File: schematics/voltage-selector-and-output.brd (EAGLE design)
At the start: 55.5 x 30.5 mm, 30 parts, among them IC1 5V, IC2 MIC2941, IC3 MCP41010P, IC5 12V, IC6 ATTINY85, Q1 2N3906

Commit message: Updated the schematics
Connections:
- net PB4: now also IC3.1
- net PB5: no longer IC3.1
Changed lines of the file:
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@@
 <contactref element="ISP" pad="1"/>
 <contactref element="IC6" pad="1"/>
-<contactref element="IC3" pad="1"/>
-<wire x1="6.35" y1="2.54" x2="19.05" y2="2.54" width="0" layer="19" extent="1-1"/>
-<wire x1="1.27" y1="17.78" x2="6.35" y2="2.54" width="0" layer="19" extent="1-1"/>
+<wire x1="6.35" y1="2.54" x2="1.27" y2="17.78" width="0" layer="19" extent="1-1"/>
 </signal>
 <signal name="PB2">
@@
 <contactref element="IC6" pad="3"/>
 <contactref element="JP4" pad="7"/>
-<wire x1="11.43" y1="2.54" x2="46.99" y2="2.54" width="0" layer="19" extent="1-1"/>
+<contactref element="IC3" pad="1"/>
+<wire x1="19.05" y1="2.54" x2="46.99" y2="2.54" width="0" layer="19" extent="1-1"/>
+<wire x1="11.43" y1="2.54" x2="19.05" y2="2.54" width="0" layer="19" extent="1-1"/>
 </signal>
 <signal name="PB0">

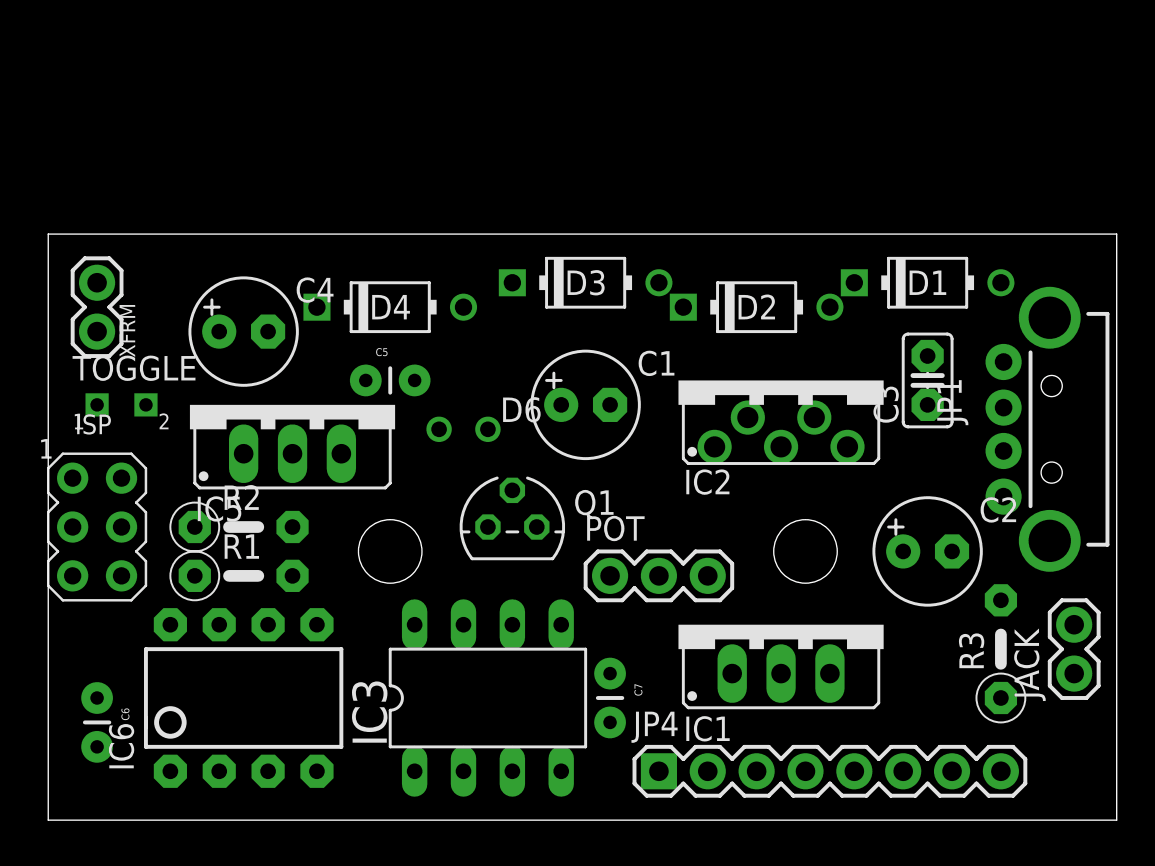
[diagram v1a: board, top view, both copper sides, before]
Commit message: Decided to remove the "adjustable" option because it was kinda useless
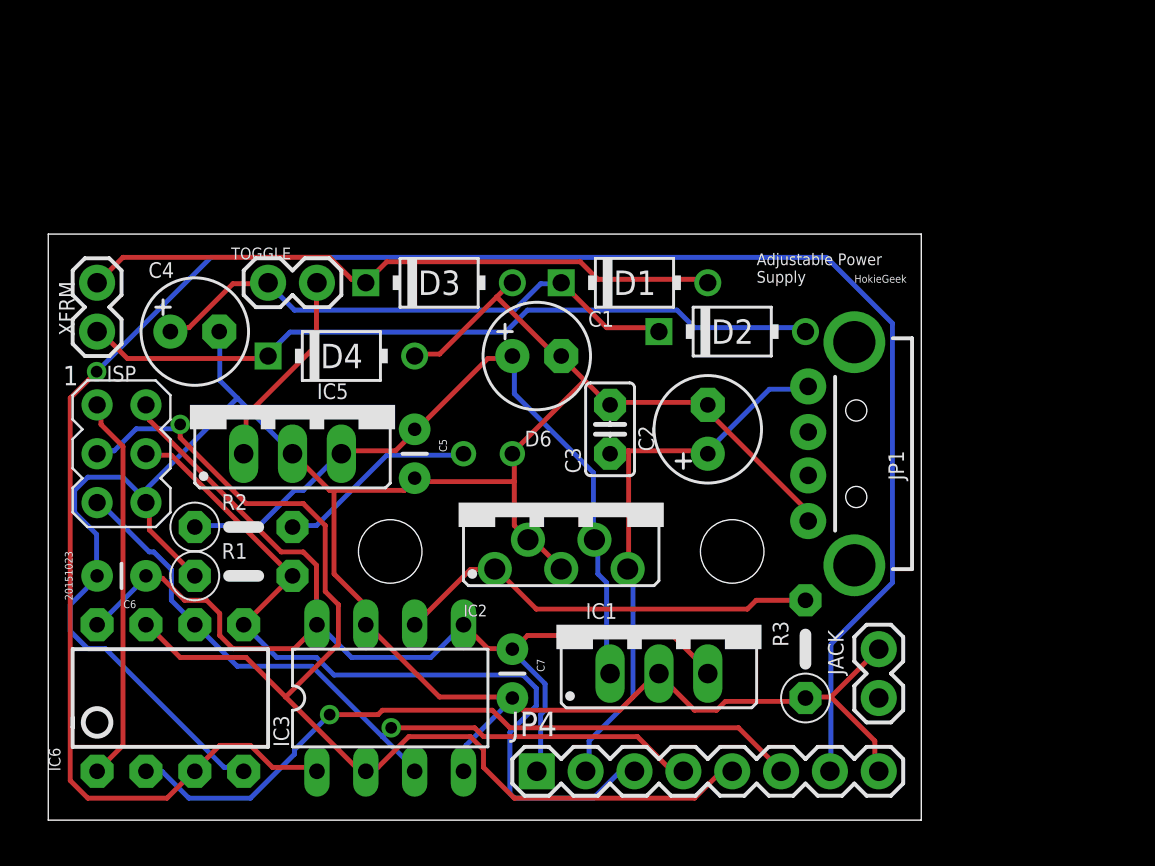
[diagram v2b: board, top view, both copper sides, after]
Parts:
- removed POT: (no value), SparkFun:1X03
- removed Q1: 2N3906, transistor-pnp:TO92
- TOGGLE: value SPST -> (none); device gm-switches:SPST -> SparkFun:1X02
- moved C3 16.7 mm to (29.2, 20.3)
- moved D1 15.2 mm to (30.5, 27.9)
- moved C2 13.1 mm to (34.3, 20.3), turned to 90 degrees
- moved IC2 13.1 mm to (26.7, 16.5)
- moved JACK 10.2 mm to (43.2, 6.35)
- moved JP1 10.2 mm to (41.9, 19.1)
- moved R3 10.2 mm to (39.4, 8.89)
- moved TOGGLE 9.92 mm to (11.4, 27.9)
- moved D3 7.62 mm to (20.3, 27.9)
- moved C6 6.84 mm to (5.08, 12.7), turned to 180 degrees
- moved IC1 6.35 mm to (31.8, 10.2)
- moved JP4 6.35 mm to (25.4, 2.54)
- moved C7 5.24 mm to (24.1, 8.89)
- moved IC3 5.08 mm to (17.8, 6.35)
- moved ISP 4.02 mm to (3.81, 19.1)
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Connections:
- removed net N$5: C1.+, C5.1, IC5.OUT, R2.1
- removed net N$6: POT.2
- removed net N$7: POT.3, Q1.1
- removed net N$8: Q1.2
- new net N$11: JACK.1
- net AGND: now also D6.K; no longer Q1.3
- net RECTIFIED_12VCC: now also C1.+, C5.1, IC5.OUT, R2.1; no longer D6.K
- net VADJ: no longer JACK.1, POT.1
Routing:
- net AGND: track 0.00 -> 148.0 mm
- net PB4: track 0.00 -> 106.7 mm, vias 0 -> 1
- net PB2: track 0.00 -> 62.3 mm, vias 0 -> 1
- net IC_VCC: track 0.00 -> 61.7 mm
- net PB0: track 0.00 -> 43.6 mm
- net PB1: track 0.00 -> 40.1 mm, vias 0 -> 1
- net N$3: track 0.00 -> 39.1 mm
- net RECTIFIED_12VCC: track 0.00 -> 38.9 mm
- net PB3: track 0.00 -> 37.0 mm, vias 0 -> 1
- net N$2: track 0.00 -> 33.9 mm
- net VADJ: track 0.00 -> 29.9 mm
- net N$9: track 0.00 -> 28.8 mm
- net N$4: track 0.00 -> 22.5 mm
- net PB5: track 0.00 -> 20.2 mm
- net N$1: track 0.00 -> 10.5 mm
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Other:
- board size 55.5 x 30.5 mm -> 45.4 x 30.5 mm
- board text added: "20151023"
- board text added: "Adjustable Power Supply"
- board text added: "HokieGeek"

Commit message: Optimizing the location of the components on the board and fixing the schematic
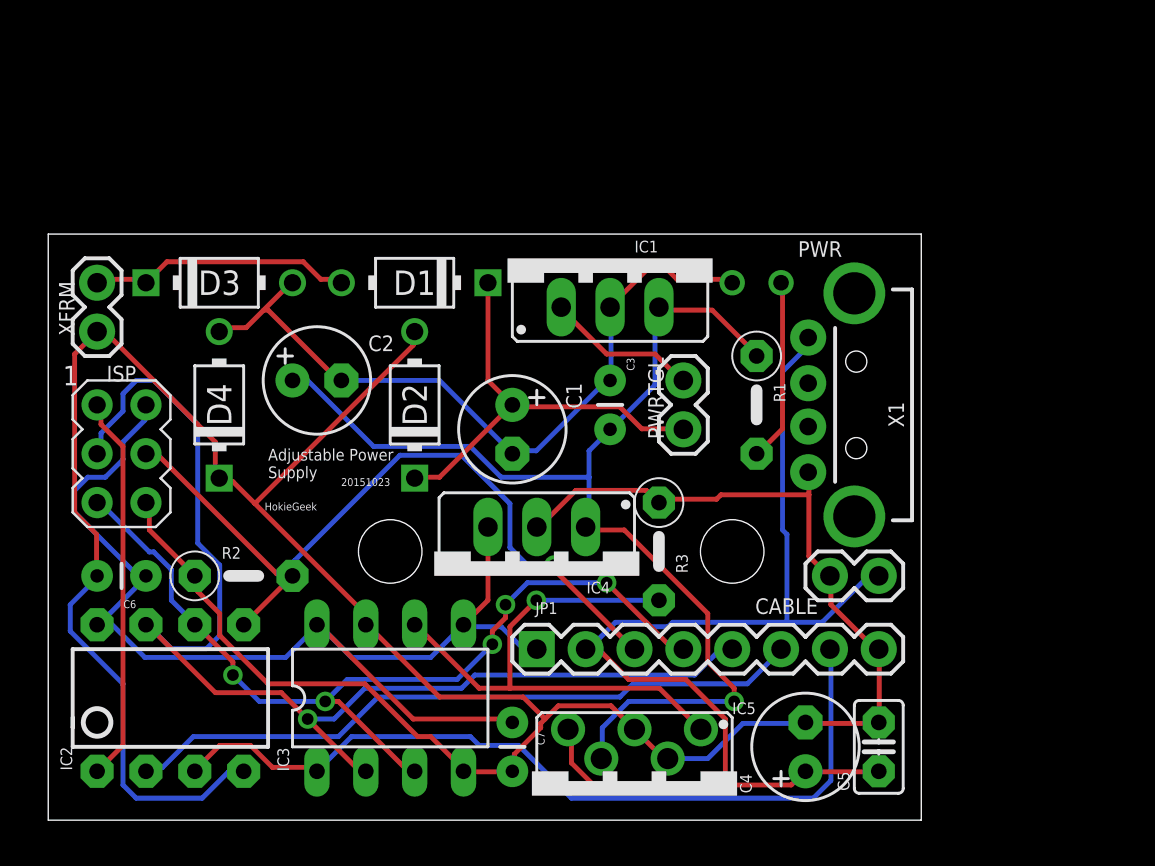
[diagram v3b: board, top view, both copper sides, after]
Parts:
- removed D6: (no value), SparkFun-LED:LED3MM-NS
- removed IC6: ATTINY85, SparkFun:DIP08
- removed JACK, TOGGLE: (no value), SparkFun:1X02
- removed JP4: (no value), SparkFun:1X08
- added CABLE, PWRTGL: (no value), SparkFun:1X02
- added IC4: 5V, v-reg:78XXS
- added PWR: (no value), SparkFun-LED:LED3MM-NS
- added X1: USB-A-H, SparkFun-Connectors:USB-A-H
- C3: device minimidi:C025-025X050 -> SparkFun-Capacitors:CAP-PTH-SMALL
- C5: device SparkFun-Capacitors:CAP-PTH-SMALL -> minimidi:C025-025X050
- IC1: value 5V -> 12V
- IC2: value MIC2941 -> ATTINY85; device bbsup:TO220-5 -> SparkFun:DIP08
- IC5: value 12V -> MIC2941; device v-reg:78XXS -> bbsup:TO220-5
- JP1: value USB-A-H -> (none); device SparkFun-Connectors:USB-A-H -> SparkFun:1X08
- R1: value 10k -> 1k
- R2: value 1k -> 10k
- moved C4 38.4 mm to (39.4, 3.81), turned to 90 degrees
- moved C5 29.2 mm to (43.2, 3.81), turned to 90 degrees
- moved R1 28.1 mm to (36.8, 21.6), turned to 270 degrees
- moved IC5 27.0 mm to (30.5, 1.27), turned to 180 degrees
- moved IC2 22.7 mm to (6.35, 6.35)
- moved C2 20.5 mm to (14.0, 22.9), turned to 0 degrees
- moved JP1 19.4 mm to (25.4, 8.89), turned to 0 degrees
- moved IC1 19.2 mm to (29.2, 29.2)
- moved D2 16.9 mm to (19.1, 21.6), turned to 90 degrees
- moved D1 11.4 mm to (19.1, 27.9), turned to 180 degrees
- moved D3 11.4 mm to (8.89, 27.9)
- moved R3 9.16 mm to (31.8, 14.0), turned to 270 degrees
- moved D4 6.84 mm to (8.89, 21.6), turned to 90 degrees
- moved C1 4.02 mm to (24.1, 20.3), turned to 270 degrees
- moved C7 3.81 mm to (24.1, 5.08)
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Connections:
- removed net N$11: JACK.1
- removed net N$3: D2.A, D4.C, XFRM.1
- new net N$5: C1.-, C2.-, C3.2, D3.A, D4.A, IC1.GND, PWR.K
- net AGND: now also CABLE.2, D2.A, D4.C, IC2.4, IC4.GND, IC5.2, IC5.3, JP1.8, R2.1, X1.GND, XFRM.1; no longer C1.-, C2.-, C3.2, D3.A, D4.A, D6.K, IC1.GND, IC2.2, IC2.3, IC5.GND, IC6.4, JACK.2, JP1.GND, JP4.8, R1.1
- net IC_VCC: now also IC2.8, IC4.OUT, JP1.1; no longer IC1.OUT, IC6.8, JP4.1
- net N$1: now also IC1.IN, PWRTGL.2; no longer IC5.IN, TOGGLE.2
- net N$10: now also PWR.A, R1.2; no longer D6.A, R2.2
- net N$4: now also IC5.1; no longer IC2.1
- net N$9: now also C1.+, PWRTGL.1; no longer C4.+, TOGGLE.1
- net PB0: now also IC2.5, JP1.3, R2.2; no longer IC6.5, JP4.3, R1.2
- net PB1: now also IC2.6, JP1.4; no longer IC6.6, JP4.4
- net PB2: now also IC2.7, JP1.5; no longer IC6.7, JP4.5
- net PB3: now also IC2.2, JP1.6; no longer IC6.2, JP4.6
- net PB4: now also IC2.3, JP1.7; no longer IC6.3, JP4.7
- net PB5: now also IC2.1; no longer IC6.1
- net RECTIFIED_12VCC: now also C2.+, C3.1, IC1.OUT, IC4.IN, IC5.4, R1.1; no longer C1.+, C5.1, IC1.IN, IC2.4, IC5.OUT, R2.1
- net VADJ: now also C4.+, C5.1, CABLE.1, IC5.5, JP1.2, X1.VBUS; no longer C2.+, C3.1, IC2.5, JP1.VBUS, JP4.2
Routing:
- net PB4: track 106.7 -> 43.6 mm, vias 1 -> 0
- net N$3: track 39.1 -> 0.00 mm
- net N$5: track 0.00 -> 39.0 mm
- net VADJ: track 29.9 -> 63.2 mm
- net RECTIFIED_12VCC: track 38.9 -> 59.2 mm, vias 0 -> 1
- net N$2: track 33.9 -> 13.8 mm
- net AGND: track 148.0 -> 158.8 mm
- net PB1: track 40.1 -> 47.1 mm, vias 1 -> 5
- net N$4: track 22.5 -> 28.6 mm, vias 0 -> 1
- net N$9: track 28.8 -> 22.9 mm
- net PB0: track 43.6 -> 40.2 mm, vias 0 -> 1
- net N$1: track 10.5 -> 7.96 mm
- net PB3: track 37.0 -> 35.7 mm, vias 1 -> 0
- net IC_VCC: track 61.7 -> 60.7 mm
- net N$10: track 10.5 -> 9.51 mm
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
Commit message: The 12v regulator was kinda too much, now that I think about it
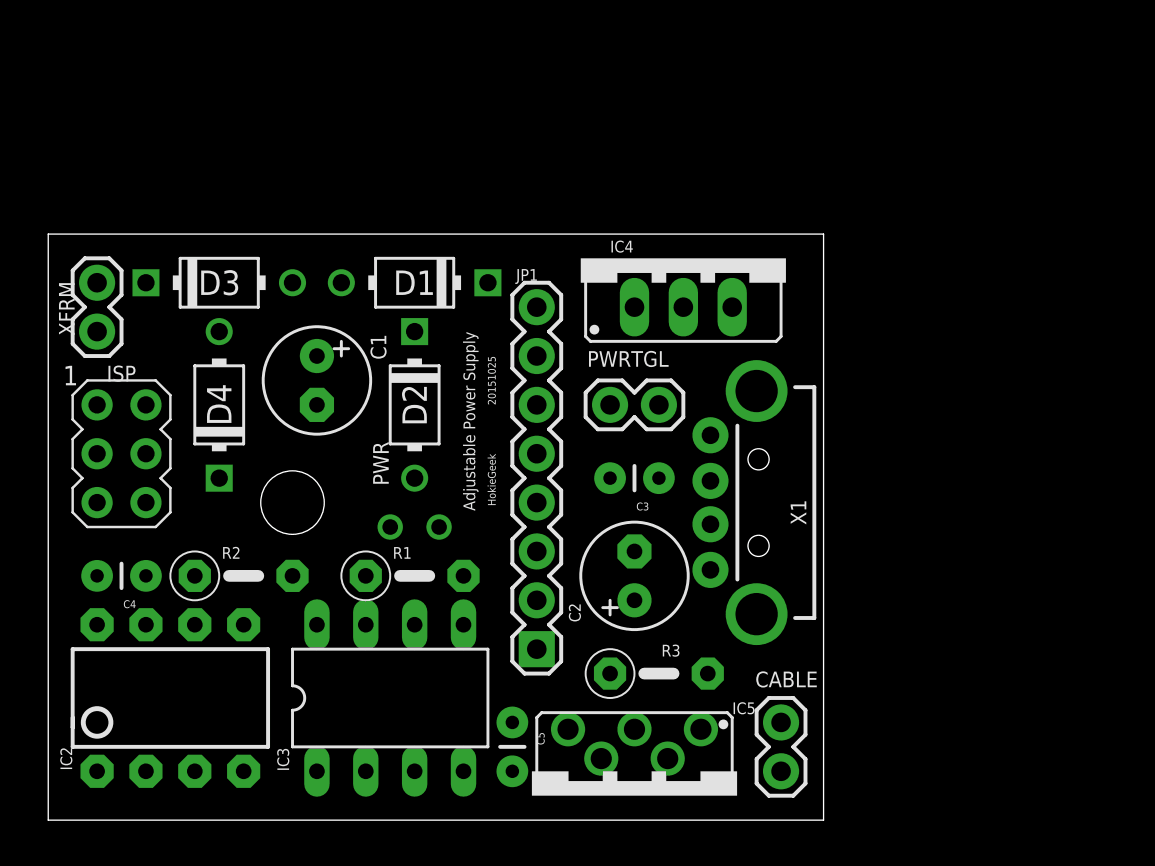
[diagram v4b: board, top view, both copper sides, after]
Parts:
- removed C6, C7: 0.1uF, SparkFun-Capacitors:CAP-PTH-SMALL
- removed IC1: 12V, v-reg:78XXS
- removed STANDOFF2: STAND-OFF, SparkFun-Electromechanical:STAND-OFF
- C4: value 47uF/25V -> 0.1uF; device minimidi:E2,5-6 -> SparkFun-Capacitors:CAP-PTH-SMALL
- C5: device minimidi:C025-025X050 -> SparkFun-Capacitors:CAP-PTH-SMALL
- moved C4 35.4 mm to (5.08, 12.7), turned to 180 degrees
- moved PWR 21.8 mm to (19.1, 15.2)
- moved R1 19.9 mm to (19.1, 12.7), turned to 0 degrees
- moved C2 19.4 mm to (30.5, 12.7), turned to 90 degrees
- moved C5 19.1 mm to (24.1, 5.08), turned to 270 degrees
- moved IC4 18.2 mm to (33.0, 29.2), turned to 0 degrees
- moved CABLE 11.4 mm to (38.1, 2.54), turned to 90 degrees
- moved C1 10.5 mm to (14.0, 22.9)
- moved X1 7.18 mm to (36.8, 16.5)
- moved R3 6.35 mm to (31.8, 7.62), turned to 0 degrees
- moved STANDOFF1 5.68 mm to (12.7, 16.5)
- moved PWRTGL 4.02 mm to (29.2, 21.6), turned to 0 degrees
- moved C3 3.59 mm to (31.8, 17.8), turned to 180 degrees
- turned D2 to 270 degrees
- turned JP1 to 90 degrees
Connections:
- removed net IC_VCC: C6.1, C7.1, IC2.8, IC3.5, IC3.8, IC4.OUT, ISP.2, JP1.1
- removed net N$1: IC1.IN, PWRTGL.2
- removed net RECTIFIED_12VCC: C2.+, C3.1, IC1.OUT, IC4.IN, IC5.4, R1.1
- new net GND: D2.A, D4.C, XFRM.1
- new net VCC: IC4.IN, IC5.4, PWRTGL.2, R1.1
- new net VIC: C4.1, C5.1, IC2.8, IC3.8, IC4.OUT, ISP.2, JP1.1
- net AGND: now also C2.-, C3.2, C4.2, IC3.5; no longer C4.-, C6.2, C7.2, D2.A, D4.C, IC3.7, XFRM.1
- net N$4: now also IC3.7
- net N$5: no longer C2.-, C3.2, IC1.GND
- net VADJ: now also C2.+, C3.1; no longer C4.+, C5.1
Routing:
- net AGND: track 158.8 -> 0.00 mm
- net VADJ: track 63.2 -> 0.00 mm
- net PB2: track 63.1 -> 0.00 mm, vias 1 -> 0
- net IC_VCC: track 60.7 -> 0.00 mm
- net RECTIFIED_12VCC: track 59.2 -> 0.00 mm, vias 1 -> 0
- net PB1: track 47.1 -> 0.00 mm, vias 5 -> 0
- net PB4: track 43.6 -> 0.00 mm
- net PB0: track 40.2 -> 0.00 mm, vias 1 -> 0
- net N$5: track 39.0 -> 0.00 mm
- net PB3: track 35.7 -> 0.00 mm
- net N$4: track 28.6 -> 0.00 mm, vias 1 -> 0
- net N$9: track 22.9 -> 0.00 mm
- net PB5: track 20.2 -> 0.00 mm
- net N$2: track 13.8 -> 0.00 mm
- net N$10: track 9.51 -> 0.00 mm
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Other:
- board size 45.4 x 30.5 mm -> 40.3 x 30.5 mm
- board text added: "20151025"
- board text removed: "20151023"

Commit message: Tweak tweak
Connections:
- new net N$1: IC3.7
- new net N$3: IC3.5
- net AGND: no longer IC3.5
- net N$4: no longer IC3.7
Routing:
- net AGND: track 0.00 -> 123.1 mm
- net VIC: track 0.00 -> 81.6 mm
- net VCC: track 0.00 -> 69.5 mm
- net PB1: track 0.00 -> 48.6 mm, vias 0 -> 1
- net PB0: track 0.00 -> 37.6 mm, vias 0 -> 1
- net PB3: track 0.00 -> 36.0 mm, vias 0 -> 1
- net PB2: track 0.00 -> 34.9 mm
- net PB4: track 0.00 -> 34.8 mm, vias 0 -> 2
- net VADJ: track 0.00 -> 34.7 mm
- net N$4: track 0.00 -> 22.3 mm
- net GND: track 0.00 -> 22.3 mm
- net N$9: track 0.00 -> 21.6 mm
- net PB5: track 0.00 -> 20.2 mm
- net N$5: track 0.00 -> 18.7 mm
- net N$2: track 0.00 -> 13.8 mm
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
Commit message: Figured out the error in my drawing, finally
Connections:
- removed net N$3: IC3.5
- removed net N$4: IC3.6, IC5.1, R3.2
- net AGND: now also IC3.5
- net N$1: now also IC3.6, IC5.1, R3.2
- net PB4: no longer JP1.7
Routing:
- net PB4: track 34.8 -> 7.58 mm, vias 2 -> 0
- net VCC: track 69.5 -> 45.8 mm
- net N$1: track 0.00 -> 22.5 mm
- net N$4: track 22.3 -> 0.00 mm
- net AGND: track 123.1 -> 106.1 mm
- net PB2: track 34.9 -> 49.5 mm
- net VIC: track 81.6 -> 68.0 mm
- net PB0: track 37.6 -> 29.1 mm, vias 1 -> 0
- net PB3: track 36.0 -> 31.2 mm, vias 1 -> 2
- net PB1: track 48.6 -> 49.0 mm, vias 1 -> 0
